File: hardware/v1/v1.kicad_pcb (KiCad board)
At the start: 2 copper layers, 139 x 99 mm, 75 parts, among them J1 AUDIO IN, J10 Close for battery power, J2 MIDI OUT, J3 MIDI IN, J4 MIDI THRU, J5 OUTPUT R, J6 OUTPUT L - MONO, J7 EXP 2, J8 EXP 1, J9 Batt In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

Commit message: Updated pcb
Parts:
- Audio In - Gain - 10k: renamed from AudioIn_gain_trim_R_1
- Gain - 10k: renamed from RV_gain_trim_R_1
- RK114GH - 10k: renamed from RV1
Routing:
- net RCH: track 34.9 -> 35.7 mm
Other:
- board text added: "Closed: battery power"
- board text added: "MIDI IN"
- board text added: "MIDI OUT"
- board text added: "MIDI THRU"
- board text added: "Raspberry Pico"
- board text added: "Volume"
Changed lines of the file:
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@@
     (property "Sheetname" "")
     (attr through_hole)
-    (fp_text reference "RV_gain_trim_R_1" (at 2.6 -2.5) (layer "F.SilkS")
+    (fp_text reference "Gain - 10k" (at 2.159 -2.413) (layer "F.SilkS")
       (effects (font (size 1 1) (thickness 0.15)))
     )
@@
     (property "Sheetname" "")
     (attr through_hole)
-    (fp_text reference "RV5" (at 6.05 -5.15 90) (layer "F.SilkS")
+    (fp_text reference "RV5" (at 11.436 -1.171 90) (layer "F.SilkS")
       (effects (font (size 1 1) (thickness 0.15)))
     )
@@
     (property "Sheetname" "")
     (attr through_hole)
-    (fp_text reference "AudioIn_gain_trim_R_1" (at 2.6 -2.5) (layer "F.SilkS")
+    (fp_text reference "Audio In - Gain - 10k" (at 2.6 -2.5) (layer "F.SilkS")
       (effects (font (size 1 1) (thickness 0.15)))
     )
@@
     (property "Sheetname" "")
     (attr through_hole)
-    (fp_text reference "RV4" (at 6.05 -5.15 90) (layer "F.SilkS")
+    (fp_text reference "RV4" (at 11.309 -1.361 90) (layer "F.SilkS")
       (effects (font (size 1 1) (thickness 0.15)))
     )
@@
     (property "Sheetname" "")
     (attr through_hole)
-    (fp_text reference "RV1" (at -3.5 -3.25 unlocked) (layer "F.SilkS")
+    (fp_text reference "RK114GH - 10k" (at -0.132 -4.13 unlocked) (layer "F.SilkS")
       (effects (font (size 1 1) (thickness 0.15)))
     )
@@
     (property "Sheetname" "")
     (attr through_hole)
-    (fp_text reference "RV3" (at 6.05 -5.15 90) (layer "F.SilkS")
+    (fp_text reference "RV3" (at 11.334 -1.237 90) (layer "F.SilkS")
       (effects (font (size 1 1) (thickness 0.15)))
     )
@@
     (effects (font (size 1 1) (thickness 0.15)))
   )
+  (gr_text "Volume\n" (at 222.25 55.499 90) (layer "F.SilkS")
+    (effects (font (size 1.5 1.5) (thickness 0.2)))
+  )
   (gr_text "1 - A\n" (at 139.5 136) (layer "F.SilkS")
     (effects (font (size 1 1) (thickness 0.15)))
   )
+  (gr_text "MIDI OUT" (at 210.439 103.632 90) (layer "F.SilkS")
+    (effects (font (size 2 2) (thickness 0.25)))
+  )
+  (gr_text "Raspberry Pico" (at 143.764 50.038) (layer "F.SilkS")
+    (effects (font (size 2 2) (thickness 0.2)))
+  )
+  (gr_text "Closed: battery power" (at 222.504 122.301 90) (layer "F.SilkS")
+    (effects (font (size 1 1) (thickness 0.15)))
+  )
+  (gr_text "MIDI THRU" (at 210.439 82.55 90) (layer "F.SilkS")
+    (effects (font (size 2 2) (thickness 0.25)))
+  )
+  (gr_text "MIDI IN" (at 104.14 91.44) (layer "F.SilkS")
+    (effects (font (size 2 2) (thickness 0.25)))
+  )
   (gr_text "3 - A" (at 195 136) (layer "F.SilkS")
     (effects (font (size 1 1) (thickness 0.15)))
@@
   (segment (start 178.7388 52.2337) (end 178.7388 46.6512) (width 0.25) (layer "B.Cu") (net 4))
   (segment (start 220.6397 61.0147) (end 219 59.375) (width 0.25) (layer "B.Cu") (net 4))
-  (segment (start 179.2678 100.0152) (end 168.9548 100.0152) (width 0.25) (layer "F.Cu") (net 5))
-  (segment (start 180.7381 98.5449) (end 179.2678 100.0152) (width 0.25) (layer "F.Cu") (net 5))
-  (segment (start 187.0738 98.5449) (end 180.7381 98.5449) (width 0.25) (layer "F.Cu") (net 5))
-  (segment (start 199.43 92.9238) (end 198.2547 92.9238) (width 0.25) (layer "F.Cu") (net 5))
-  (segment (start 197.0287 94.1498) (end 191.4689 94.1498) (width 0.25) (layer "F.Cu") (net 5))
-  (segment (start 198.2547 92.9238) (end 197.0287 94.1498) (width 0.25) (layer "F.Cu") (net 5))
-  (segment (start 191.4689 94.1498) (end 187.0738 98.5449) (width 0.25) (layer "F.Cu") (net 5))
-  (via (at 168.9548 100.0152) (size 0.8) (drill 0.4) (layers "F.Cu" "B.Cu") (net 5))
-  (segment (start 167.875 101.095) (end 168.9548 100.0152) (width 0.25) (layer "B.Cu") (net 5))
+  (segment (start 168.275 99.314) (end 179.969 99.314) (width 0.25) (layer "F.Cu") (net 5))
+  (segment (start 191.4689 94.1498) (end 197.0287 94.1498) (width 0.25) (layer "F.Cu") (net 5))
+  (segment (start 198.2547 92.9238) (end 199.43 92.9238) (width 0.25) (layer "F.Cu") (net 5))
+  (segment (start 179.969 99.314) (end 180.7381 98.5449) (width 0.25) (layer "F.Cu") (net 5))
+  (segment (start 180.7381 98.5449) (end 187.0738 98.5449) (width 0.25) (layer "F.Cu") (net 5))
+  (segment (start 187.0738 98.5449) (end 191.4689 94.1498) (width 0.25) (layer "F.Cu") (net 5))
+  (segment (start 197.0287 94.1498) (end 198.2547 92.9238) (width 0.25) (layer "F.Cu") (net 5))
+  (via (at 168.275 99.314) (size 0.8) (drill 0.4) (layers "F.Cu" "B.Cu") (net 5))
+  (segment (start 167.875 101.095) (end 168.275 100.695) (width 0.25) (layer "B.Cu") (net 5))
+  (segment (start 168.275 100.695) (end 168.275 99.314) (width 0.25) (layer "B.Cu") (net 5))
   (segment (start 199.3794 95.4744) (end 199.43 95.4238) (width 0.25) (layer "F.Cu") (net 6))
   (segment (start 193.5 95.4744) (end 199.3794 95.4744) (width 0.25) (layer "F.Cu") (net 6))
@@
   (segment (start 120.024 45.0964) (end 120.024 47.1957) (width 0.25) (layer "B.Cu") (net 80))
   (segment (start 123.3642 89.8858) (end 113.5 99.75) (width 0.25) (layer "B.Cu") (net 80))
-  (segment (start 200.9148 99.0452) (end 180.9454 99.0452) (width 0.25) (layer "F.Cu") (net 82))
-  (segment (start 204.15 95.81) (end 200.9148 99.0452) (width 0.25) (layer "F.Cu") (net 82))
-  (segment (start 180.9454 99.0452) (end 179.0623 100.9283) (width 0.25) (layer "F.Cu") (net 82))
+  (segment (start 180.0416 99.949) (end 179.0623 100.9283) (width 0.25) (layer "F.Cu") (net 82))
+  (segment (start 200.011 99.949) (end 180.0416 99.949) (width 0.25) (layer "F.Cu") (net 82))
   (segment (start 179.0623 100.9283) (end 133.5983 100.9283) (width 0.25) (layer "F.Cu") (net 82))
+  (segment (start 204.15 95.81) (end 200.011 99.949) (width 0.25) (layer "F.Cu") (net 82))
   (segment (start 128.8524 90.73) (end 122.5765 84.4541) (width 0.25) (layer "F.Cu") (net 82))
   (segment (start 133.5983 100.9283) (end 131.02 98.35) (width 0.25) (layer "F.Cu") (net 82))

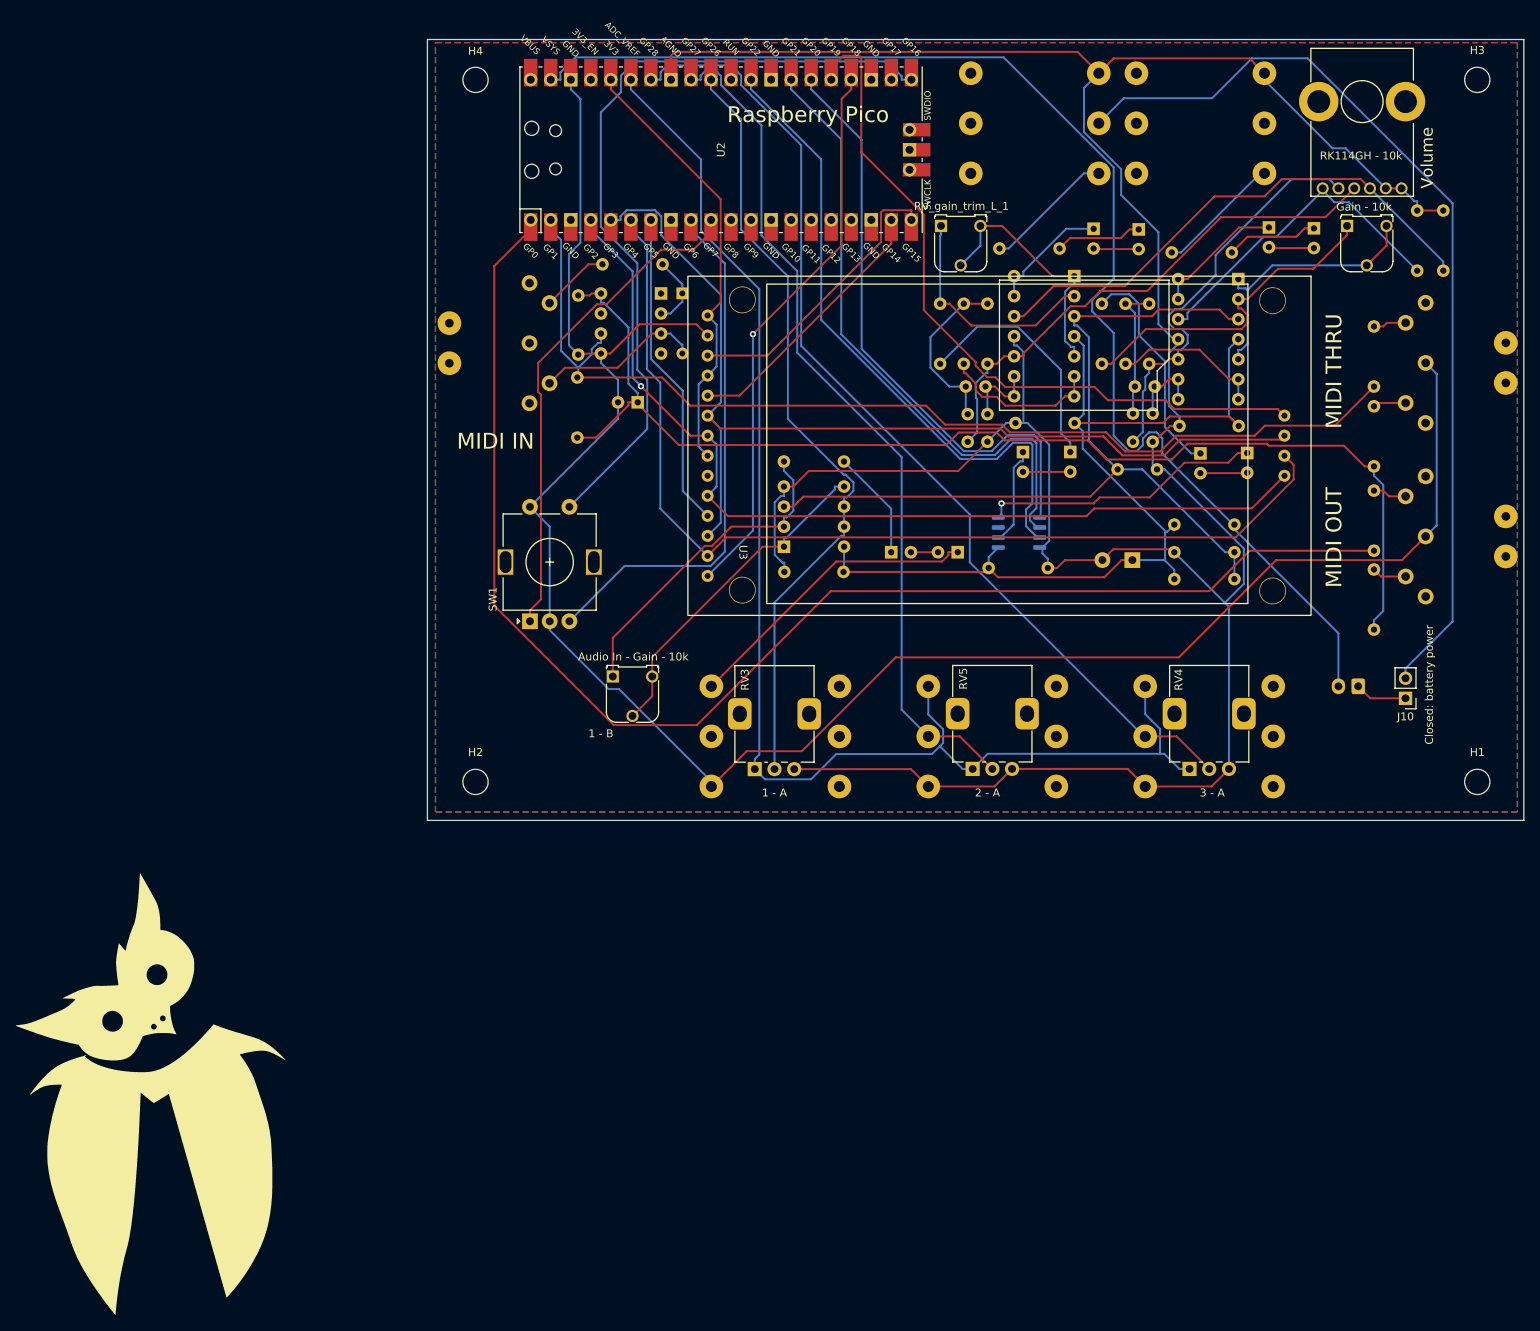
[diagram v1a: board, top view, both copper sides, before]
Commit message: Moved optocoupler to the digital side, labels placement
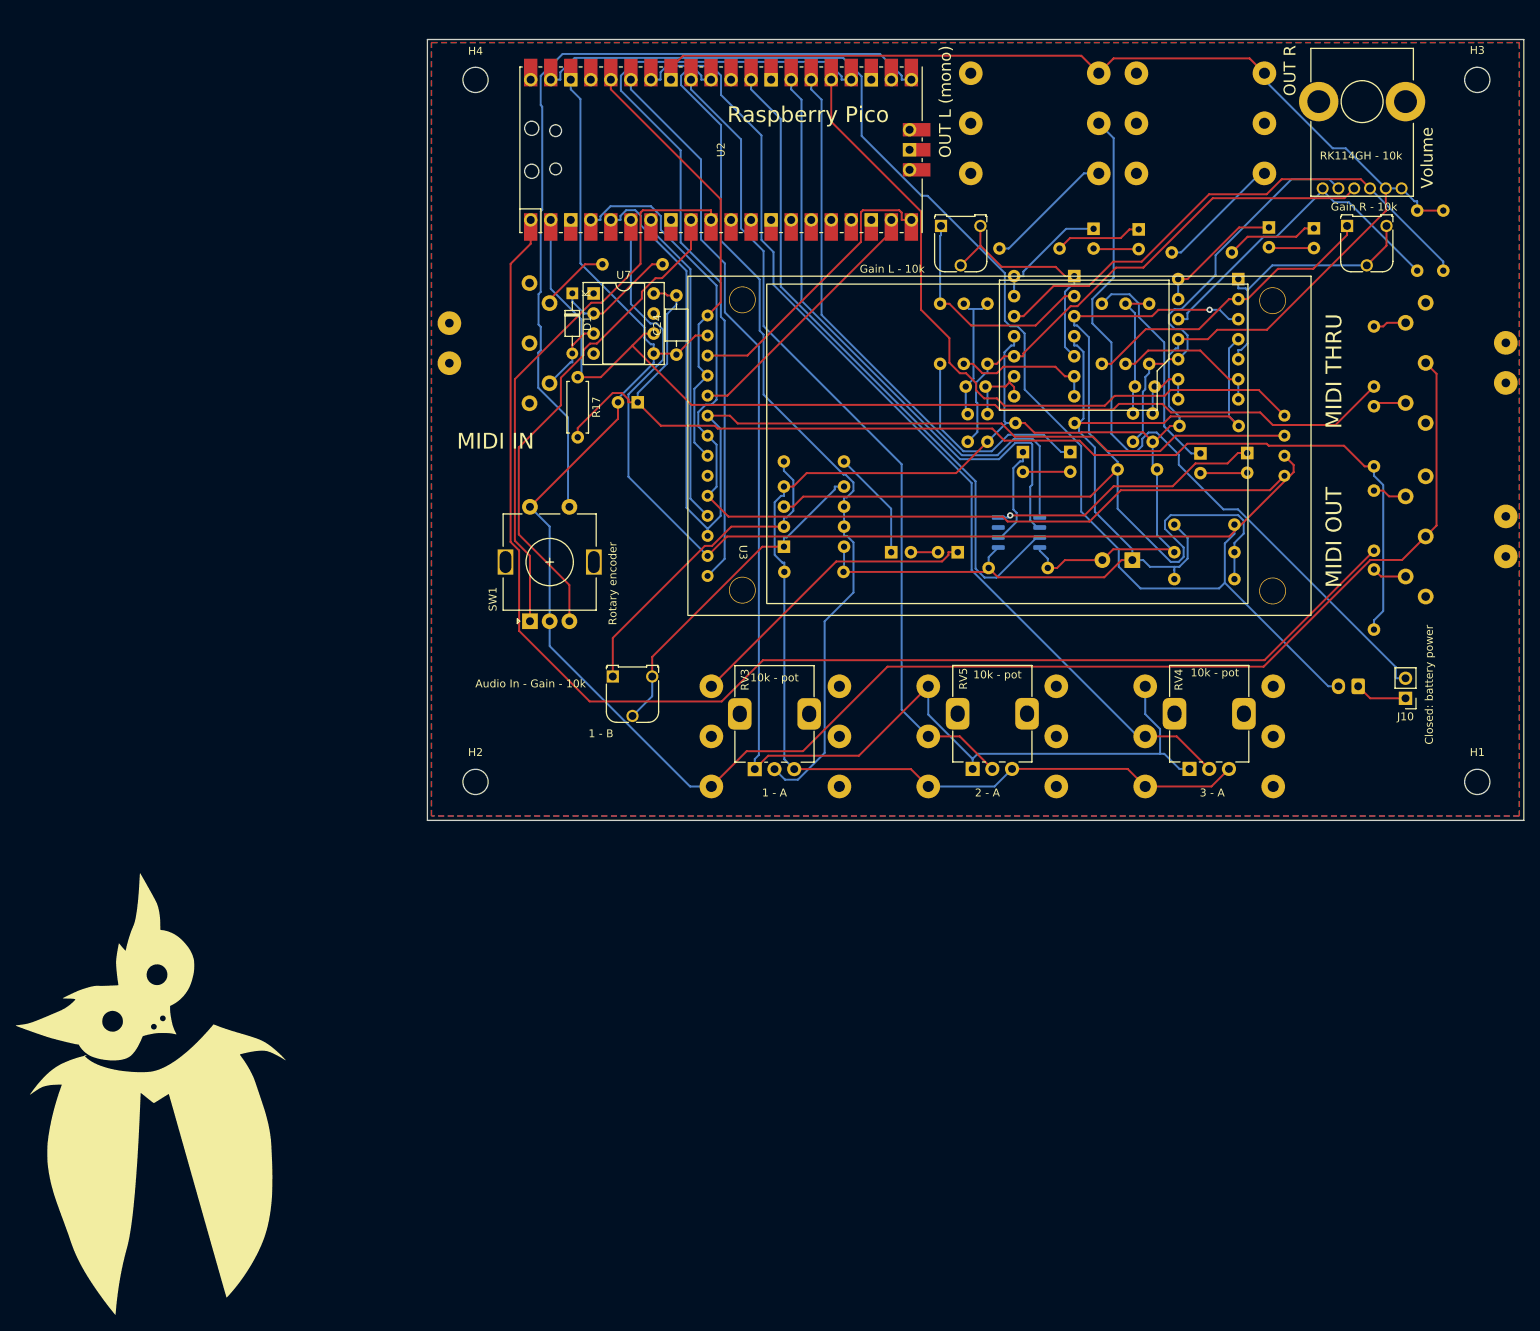
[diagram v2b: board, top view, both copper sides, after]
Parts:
- C24, D1, R17, U7: moved to F.Cu
- Gain L - 10k: renamed from RV_gain_trim_L_1
- Gain R - 10k: renamed from Gain - 10k
- moved D1 13.9 mm to (113.9, 72.7)
- moved C24 12.4 mm to (127.1, 80.5)
- moved U7 8.55 mm to (116.6, 72.7), turned to 0 degrees
- moved R17 0.07 mm to (114.6, 83.3)
- renumbered U1 to PT8211
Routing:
- net Net-(U2-Pad24): track 70.5 -> 100.9 mm, vias 1 -> 0
- net GNDA: track 380.2 -> 358.1 mm
- net Net-(J10-Pad2): track 118.6 -> 96.4 mm
- net virtual_mass: track 110.4 -> 128.2 mm, vias 0 -> 1
- net Net-(D1-Pad2): track 21.1 -> 9.51 mm
- net Net-(RV3-Pad2): track 99.6 -> 111.2 mm
- net Net-(U2-Pad5): track 129.5 -> 140.5 mm
- net Net-(U2-Pad4): track 119.6 -> 128.5 mm, vias 1 -> 0
- net Net-(D1-Pad1): track 9.14 -> 15.7 mm
- net Net-(SW1-PadA): track 63.8 -> 70.2 mm
- net GND: track 252.6 -> 246.5 mm
- net Net-(SW1-PadS1): track 101.0 -> 106.6 mm
- net Net-(C14-Pad1): track 21.9 -> 17.4 mm
- net filtered_vcc: track 120.9 -> 125.2 mm
- net Net-(R16-Pad1): track 177.8 -> 173.6 mm
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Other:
- board text added: "10"
- board text added: "1000p"
- board text added: "1000u"
- board text added: "100n"
- board text added: "10k"
- board text added: "10k - pot"
- board text added: "10u"
- board text added: "1k"
- board text added: "22k (fc 10k) 10k (fc 16k)"
- board text added: "33"
- board text added: "680p"
- board text added: "680p (op)"
- board text added: "AUDIO IN"
- board text added: "EXP 1"
- board text added: "EXP 2"
- board text added: "OUT L (mono)"
- board text added: "OUT R"
- board text added: "Rotary encoder"
- board text added: "TL074"

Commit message: Labelling pcb - placed the owl
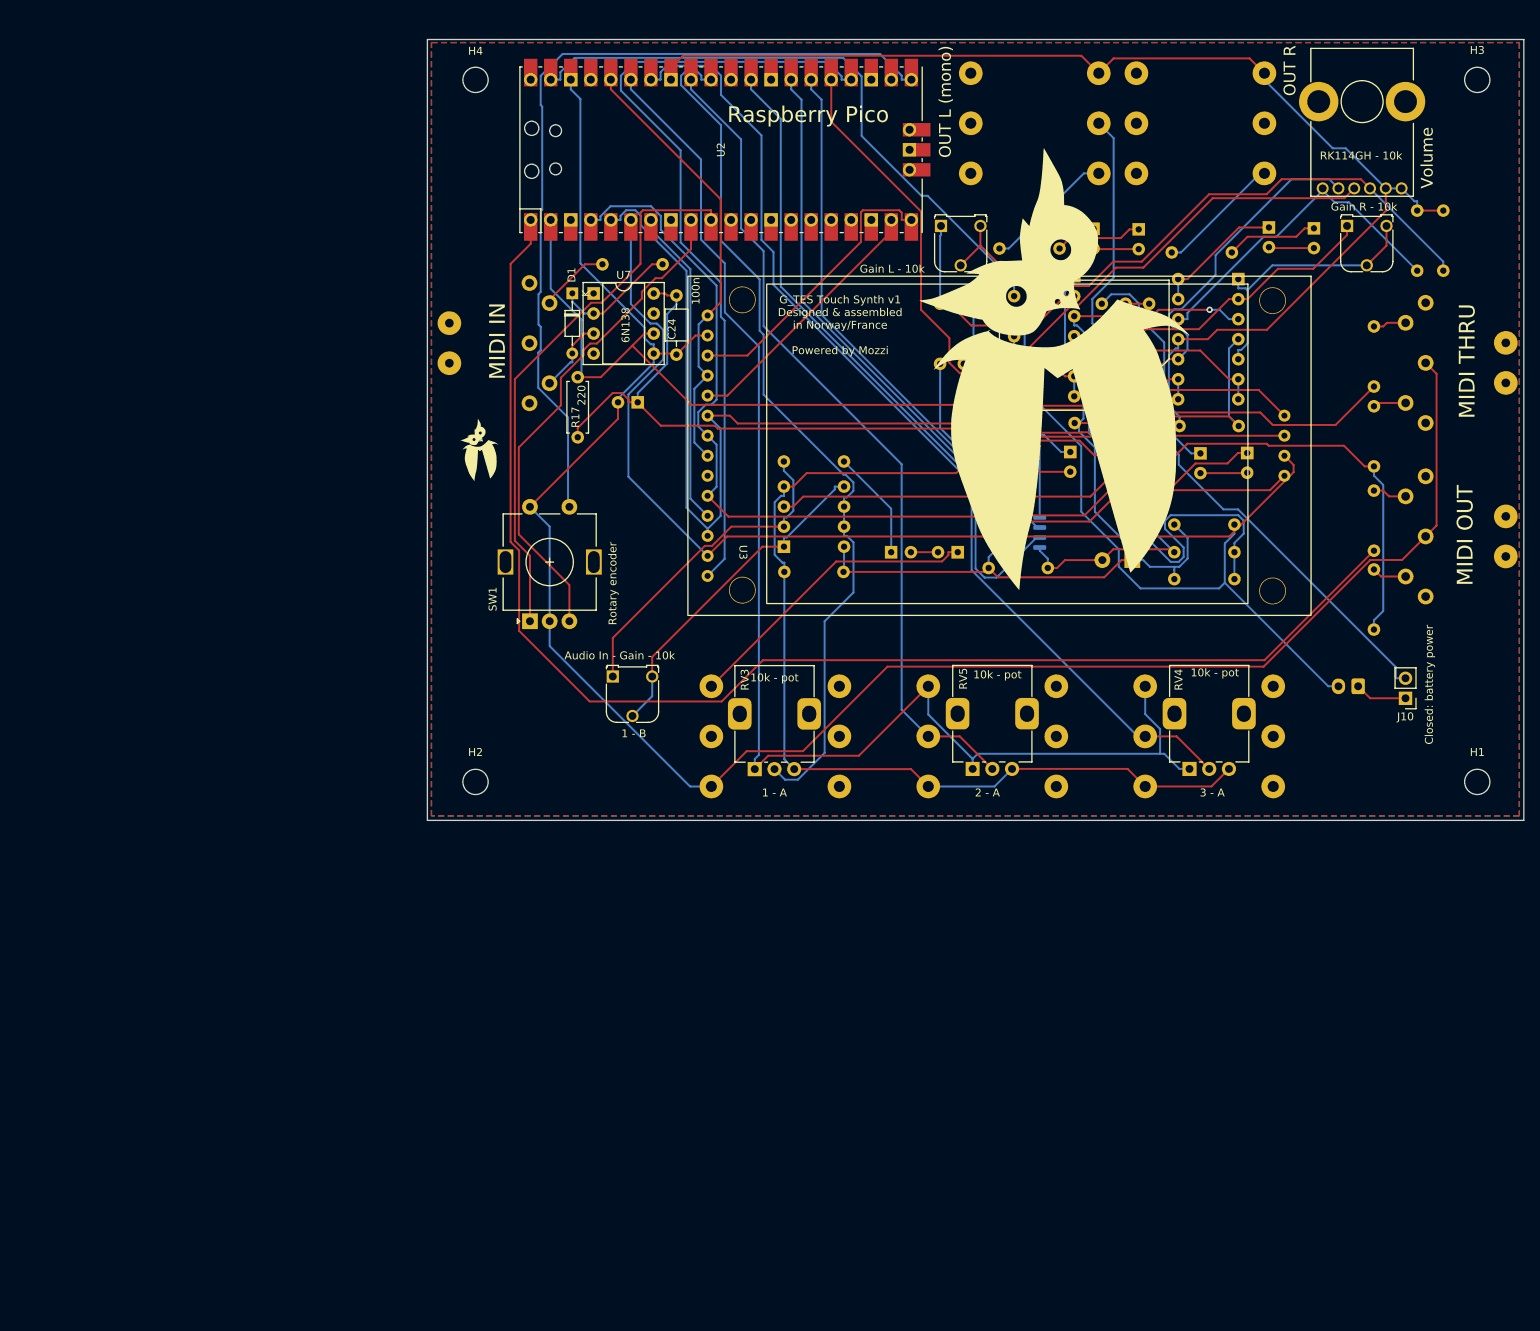
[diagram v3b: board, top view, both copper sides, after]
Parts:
- removed the G*** at (60.5, 175.5)
- added G***: LOGO, PCB_symbols:owl_F_50x70, F.Cu at (175.1, 83.6)
- added G***: LOGO, PCB_symbols:owl_7x10, F.Cu at (102.1, 92.7)
- added G***: LOGO, PCB_symbols:owl_F_50x70, B.Cu at (110.5, 118.1)
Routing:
- net RCH: track 34.9 -> 37.4 mm
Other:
- board text added: "100u"
- board text added: "220"
- board text added: "6N138"
- board text added: "G_TES Touch Synth v1 Designed & assembled in Norway/France Powered by Mozzi"
- board text added: "TL072"
